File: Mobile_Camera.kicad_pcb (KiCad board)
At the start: 2 copper layers, 79 parts, among them J1 SWD_header, J2 DVP_24_pin, J3 Micro_SD_card, J4 Antenna_connector, J5 Micro_SIM_card, J6 USB_C_receptacle, Q1 Q_NPN, SW1 Switch_reset, SW2 Switch_power_on, U1 STM32H753VIT6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

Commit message: Partial layout
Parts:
- SW1: value Switch_reset -> SW_Power_On
- SW2: value Switch_power_on -> SW_Reset
- moved J5 108.0 mm to (149.6, 115.5), turned to -90 degrees
- moved J6 71.2 mm to (46.8, 133.2)
- moved C24 66.3 mm to (94.5, 137.0)
- moved C23 65.0 mm to (90.0, 134.7), turned to 90 degrees
- moved C22 62.7 mm to (41.6, 126.7), turned to 90 degrees
- moved C25 60.6 mm to (96.7, 132.2), turned to -90 degrees
- moved C9 59.9 mm to (-17.8, 79.2)
- moved C3 58.6 mm to (-17.5, 68.2)
- moved R12 55.8 mm to (100.2, 132.2), turned to 90 degrees
- moved R13 52.7 mm to (98.5, 132.2), turned to -90 degrees
- moved C26 52.1 mm to (93.2, 127.0), turned to 180 degrees
- moved R14 51.7 mm to (95.7, 135.0), turned to 180 degrees
- moved C7 50.1 mm to (26.2, 92.2), turned to 180 degrees
- moved L1 49.6 mm to (92.5, 130.5)
- moved D5 49.2 mm to (43.6, 126.7), turned to 90 degrees
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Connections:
- J2 pad MP: (no net) -> GND
- J5 pad SH: (no net) -> GND
- SW1 pad 2: GND -> /PWR
- SW2 pad 2: GND -> /NRST

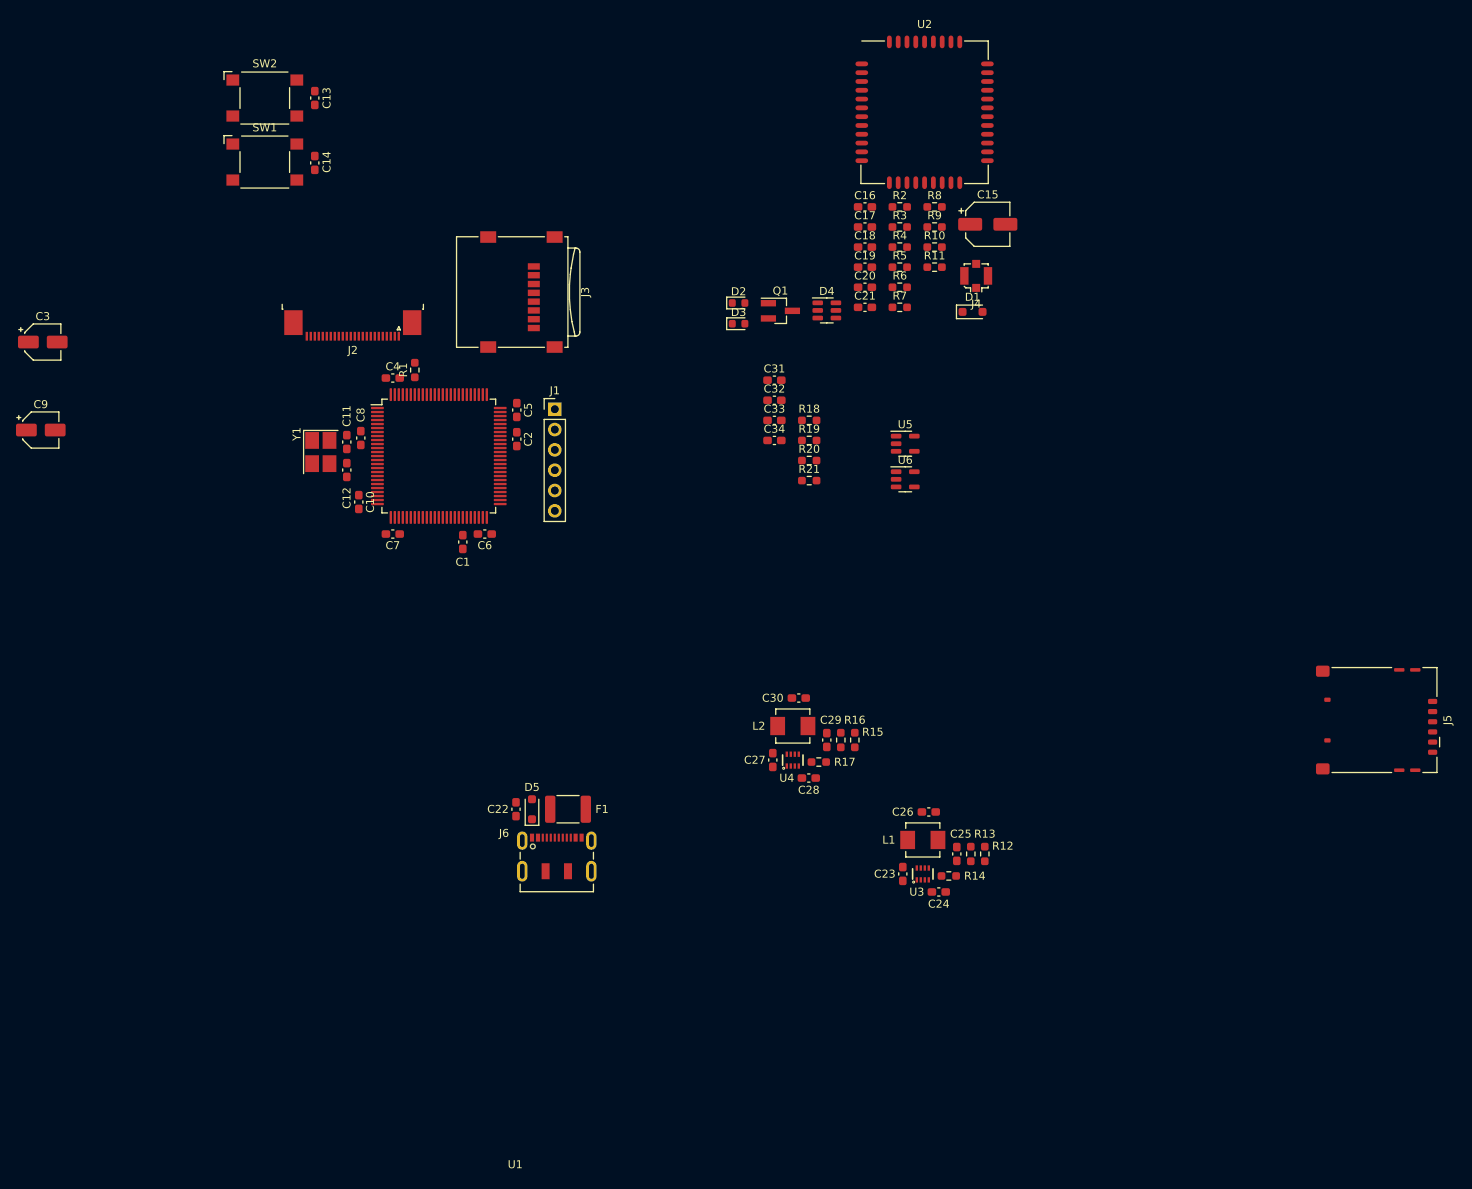
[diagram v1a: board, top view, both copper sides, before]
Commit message: Add layout and ednge cut
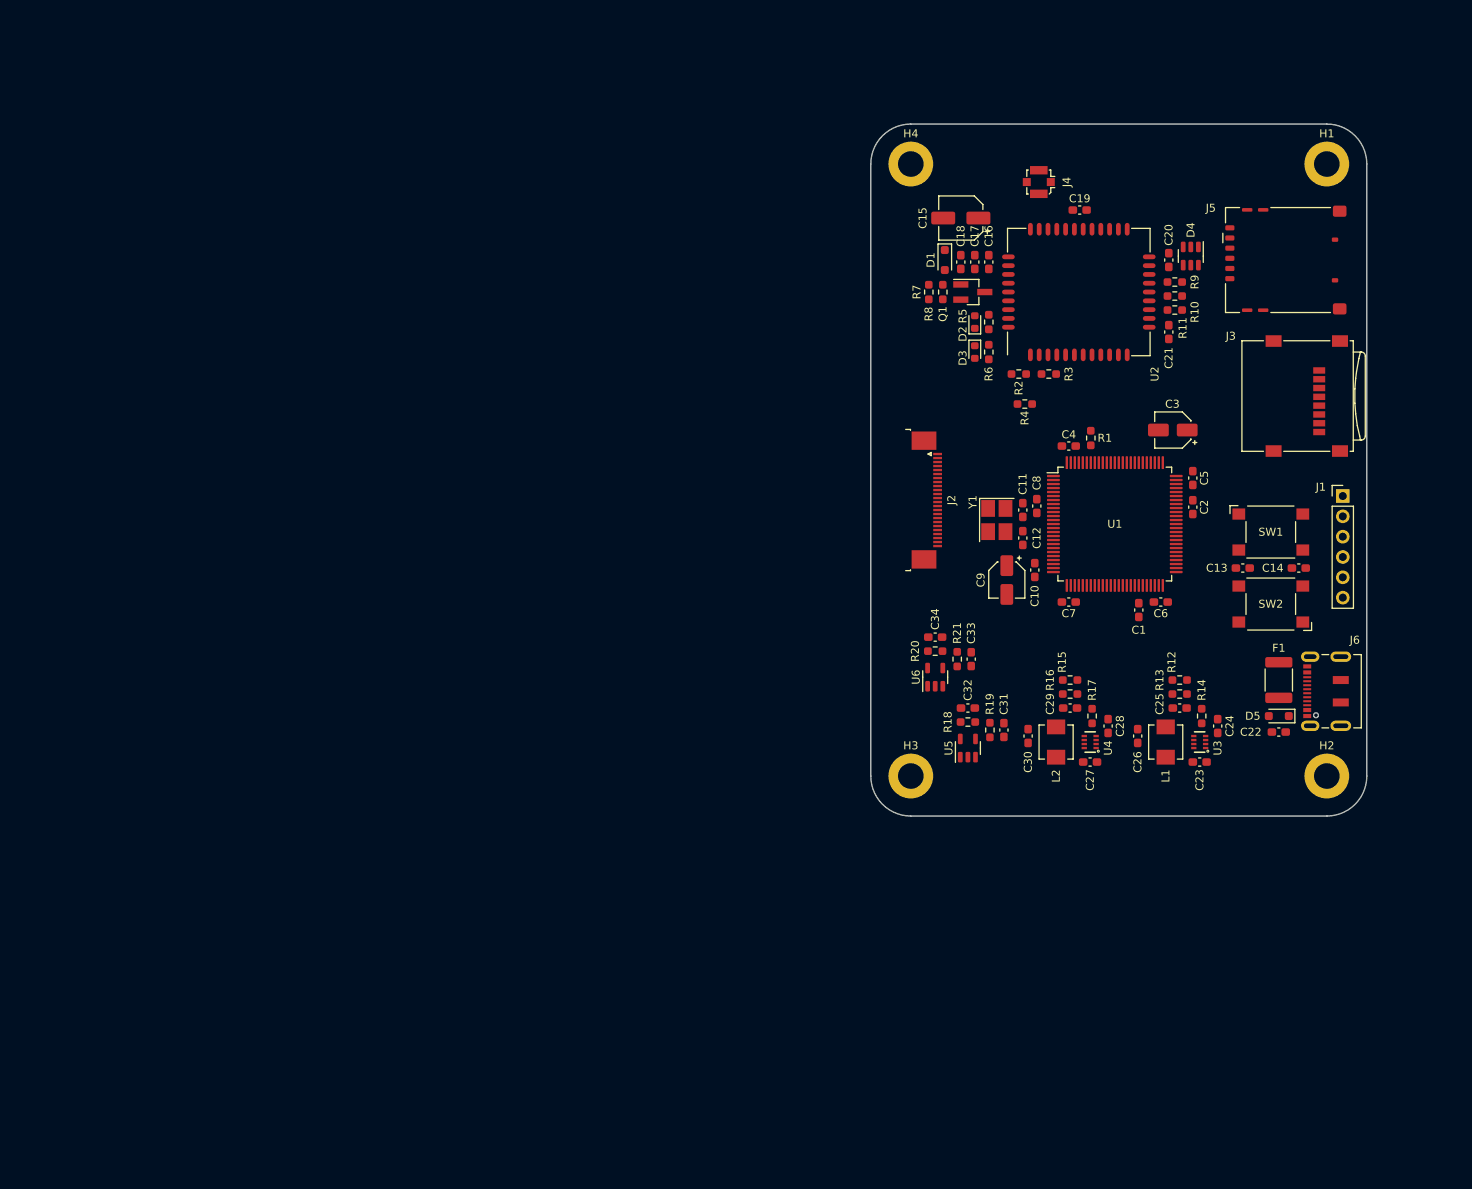
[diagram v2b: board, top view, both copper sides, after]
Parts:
- added H1: MountingHole_Pad, MountingHole:MountingHole_3.2mm_M3_DIN965_Pad, F.Cu at (143.0, 46.0)
- added H2: MountingHole_Pad, MountingHole:MountingHole_3.2mm_M3_DIN965_Pad, F.Cu at (143.0, 122.5)
- added H3: MountingHole_Pad, MountingHole:MountingHole_3.2mm_M3_DIN965_Pad, F.Cu at (91.0, 122.5)
- added H4: MountingHole_Pad, MountingHole:MountingHole_3.2mm_M3_DIN965_Pad, F.Cu at (91.0, 46.0)
- moved C3 141.7 mm to (123.8, 79.2), turned to 180 degrees
- moved SW2 140.8 mm to (136.0, 101.0), turned to 180 degrees
- moved SW1 134.0 mm to (136.0, 92.0)
- moved C14 133.0 mm to (139.5, 96.5), turned to 180 degrees
- moved C13 130.0 mm to (132.5, 96.5), turned to 0 degrees
- moved C9 122.2 mm to (103.0, 98.0), turned to -90 degrees
- moved J6 99.2 mm to (143.6, 111.9), turned to 90 degrees
- moved J1 99.1 mm to (145.0, 87.5)
- moved J3 99.0 mm to (140.5, 75.0)
- moved C22 95.8 mm to (137.0, 117.0), turned to 180 degrees
- moved D5 94.1 mm to (137.0, 115.0), turned to 180 degrees
- moved F1 90.3 mm to (137.0, 110.5), turned to -90 degrees
- moved C1 84.9 mm to (119.5, 101.8)
- moved C10 84.9 mm to (106.5, 96.8)
- moved C11 84.9 mm to (105.0, 89.2)
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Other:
- board outline added: 62 x 86.5 mm

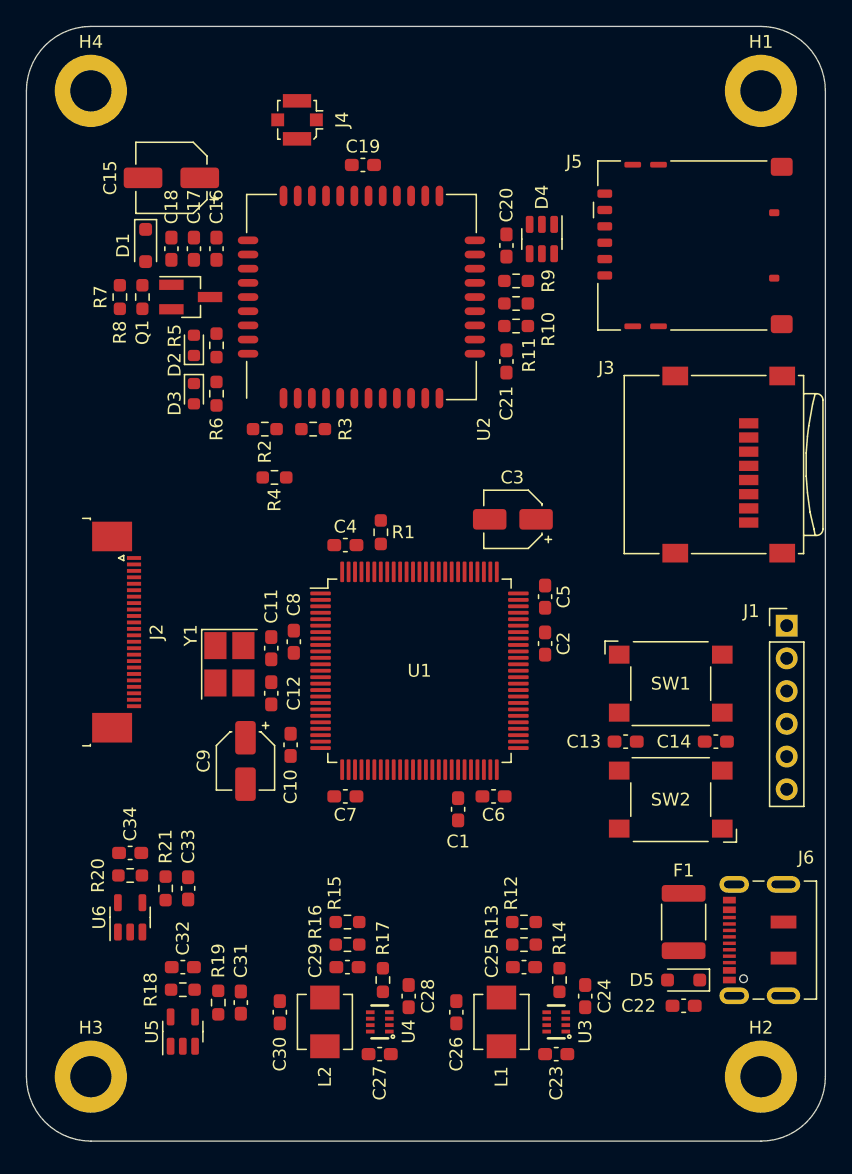
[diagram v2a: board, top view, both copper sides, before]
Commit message: Add power delivery routing
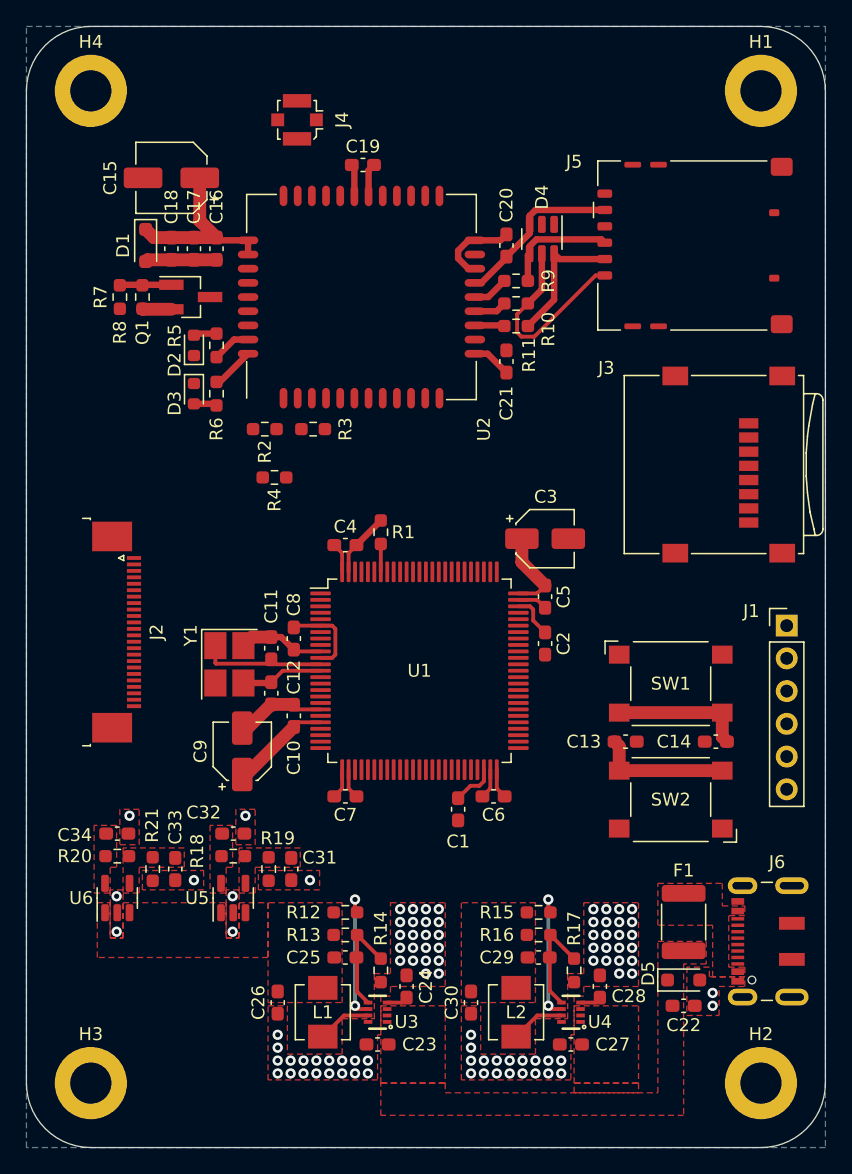
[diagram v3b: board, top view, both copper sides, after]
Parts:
- moved C27 14.9 mm to (128.2, 120.0)
- moved C28 14.9 mm to (130.5, 115.5)
- moved C29 14.9 mm to (125.8, 113.2)
- moved C30 14.9 mm to (120.5, 116.8)
- moved L2 14.9 mm to (124.0, 117.5)
- moved R15 14.9 mm to (125.8, 109.8)
- moved R16 14.9 mm to (125.8, 111.5)
- moved R17 14.9 mm to (128.5, 114.2)
- moved U4 14.9 mm to (128.3, 117.5)
- moved C24 13.9 mm to (115.5, 115.5)
- moved C23 13.9 mm to (113.2, 120.0)
- moved C25 13.9 mm to (110.8, 113.2)
- moved C26 13.9 mm to (105.5, 116.8)
- moved L1 13.9 mm to (109.0, 117.5)
- moved R12 13.9 mm to (110.8, 109.8)
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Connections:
- J6 pad A6: unconnected-(J6-D+-PadA6) -> (no net)
- J6 pad A7: unconnected-(J6-D--PadA7) -> (no net)
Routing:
- net GND: track 0.00 -> 45.7 mm, vias 0 -> 90
- net +3V3: track 0.00 -> 28.1 mm
- net Net-(D4-IO4): track 0.00 -> 15.8 mm
- net +4V: track 0.00 -> 14.6 mm
- net /SIM/SIM_VDD: track 0.00 -> 13.3 mm
- net Net-(D4-IO5): track 0.00 -> 10.6 mm
- net Net-(U4-PG): track 0.00 -> 10.4 mm, vias 0 -> 2
- net Net-(U3-PG): track 0.00 -> 10.4 mm, vias 0 -> 2
- net /PWR: track 0.00 -> 10.4 mm
- net /NRST: track 0.00 -> 10.4 mm
- net /PH0: track 0.00 -> 9.83 mm
- net Net-(D4-IO3): track 0.00 -> 8.91 mm
- net Net-(U4-FB): track 0.00 -> 8.25 mm
- net Net-(U3-FB): track 0.00 -> 8.20 mm
- net /PH1: track 0.00 -> 6.38 mm
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- added copper zone on F.Cu, net +1V35
- added copper zone on F.Cu, net +2V8
- added copper zone on F.Cu, net +3V3
- added copper zone on F.Cu, net +4V
- added copper zone on F.Cu, net +5V
- added copper zone on B.Cu, net GND
- added copper zone on F.Cu, net GND
- added copper zone on F.Cu, net Net-(F1-Pad1)
- added copper zone on F.Cu, net Net-(U5-ADJ)
- added copper zone on F.Cu, net Net-(U6-ADJ)
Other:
- board size 62 x 86.5 mm -> 62 x 87 mm

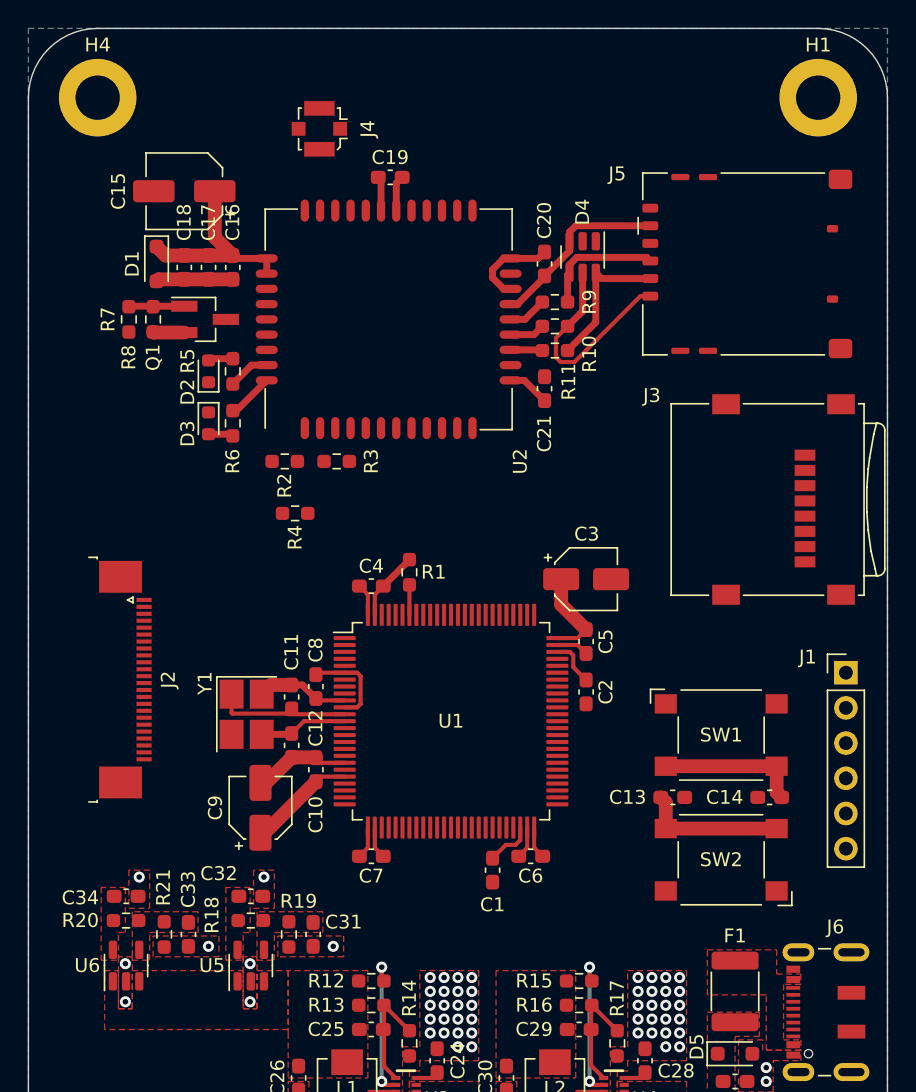
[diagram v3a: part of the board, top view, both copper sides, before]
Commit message: Add controlled impedence trace
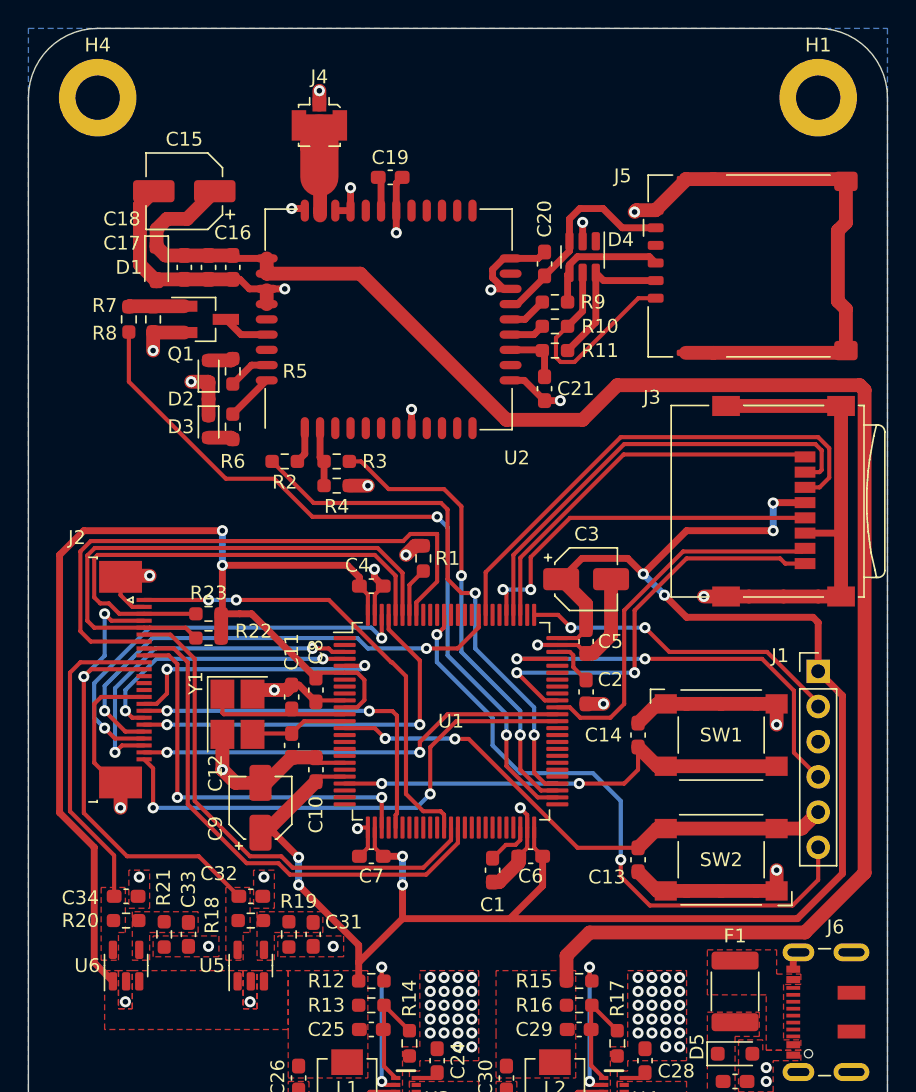
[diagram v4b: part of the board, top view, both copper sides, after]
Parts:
- added R22: 4.7k, Resistor_SMD:R_0603_1608Metric_Pad0.98x0.95mm_HandSolder, F.Cu at (99.0, 85.0)
- added R23: 4.7k, Resistor_SMD:R_0603_1608Metric_Pad0.98x0.95mm_HandSolder, F.Cu at (99.0, 83.2)
- moved C14 10.5 mm to (130.0, 92.0), turned to 90 degrees
- moved C13 5.15 mm to (130.0, 101.0), turned to -90 degrees
- moved R4 3.61 mm to (108.2, 74.0)
- moved J1 2.00 mm to (143.0, 87.4)
- moved R1 1.41 mm to (114.5, 79.2)
- moved Y1 0.66 mm to (101.1, 90.5)
- moved J5 0.42 mm to (137.9, 58.1)
- moved C8 0.25 mm to (106.8, 88.8)
- moved D3 0.25 mm to (99.0, 69.8)
- moved J4 0.25 mm to (107.0, 48.0), turned to 180 degrees
- moved R6 0.25 mm to (100.8, 69.8)
- moved J3 0.12 mm to (140.5, 75.1)
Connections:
- J6 pad A6: (no net) -> unconnected-(J6-D+-PadA6)
- J6 pad A7: (no net) -> unconnected-(J6-D--PadA7)
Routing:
- net +3V3: track 28.1 -> 219.1 mm, vias 0 -> 10
- net GND: track 45.7 -> 217.8 mm, vias 90 -> 114
- net +4V: track 14.6 -> 125.4 mm
- net /SIM_PWR: track 0.00 -> 54.5 mm, vias 0 -> 2
- net /SWO: track 0.00 -> 45.9 mm, vias 0 -> 2
- net /DCMI_VSYNC: track 0.00 -> 43.4 mm
- net /I2C_SCL: track 0.00 -> 39.8 mm
- net /SIM_TX: track 0.00 -> 38.3 mm, vias 0 -> 2
- net /DCMI_D0: track 0.00 -> 37.5 mm, vias 0 -> 2
- net /DCMI_PWDN: track 0.00 -> 37.5 mm
- net /DCMI_RESET: track 0.00 -> 36.9 mm
- net /SD_CMD: track 0.00 -> 36.4 mm
- net +2V8: track 0.00 -> 36.3 mm, vias 0 -> 2
- net /I2C_SDA: track 0.00 -> 35.9 mm
- net /DCMI_D5: track 0.00 -> 35.5 mm, vias 0 -> 2
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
